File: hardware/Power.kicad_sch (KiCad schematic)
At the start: 41 parts, among them IC1 3.3V/0.5A, IC2 TPS54202HDDCR, U12 LMR33640DDDA

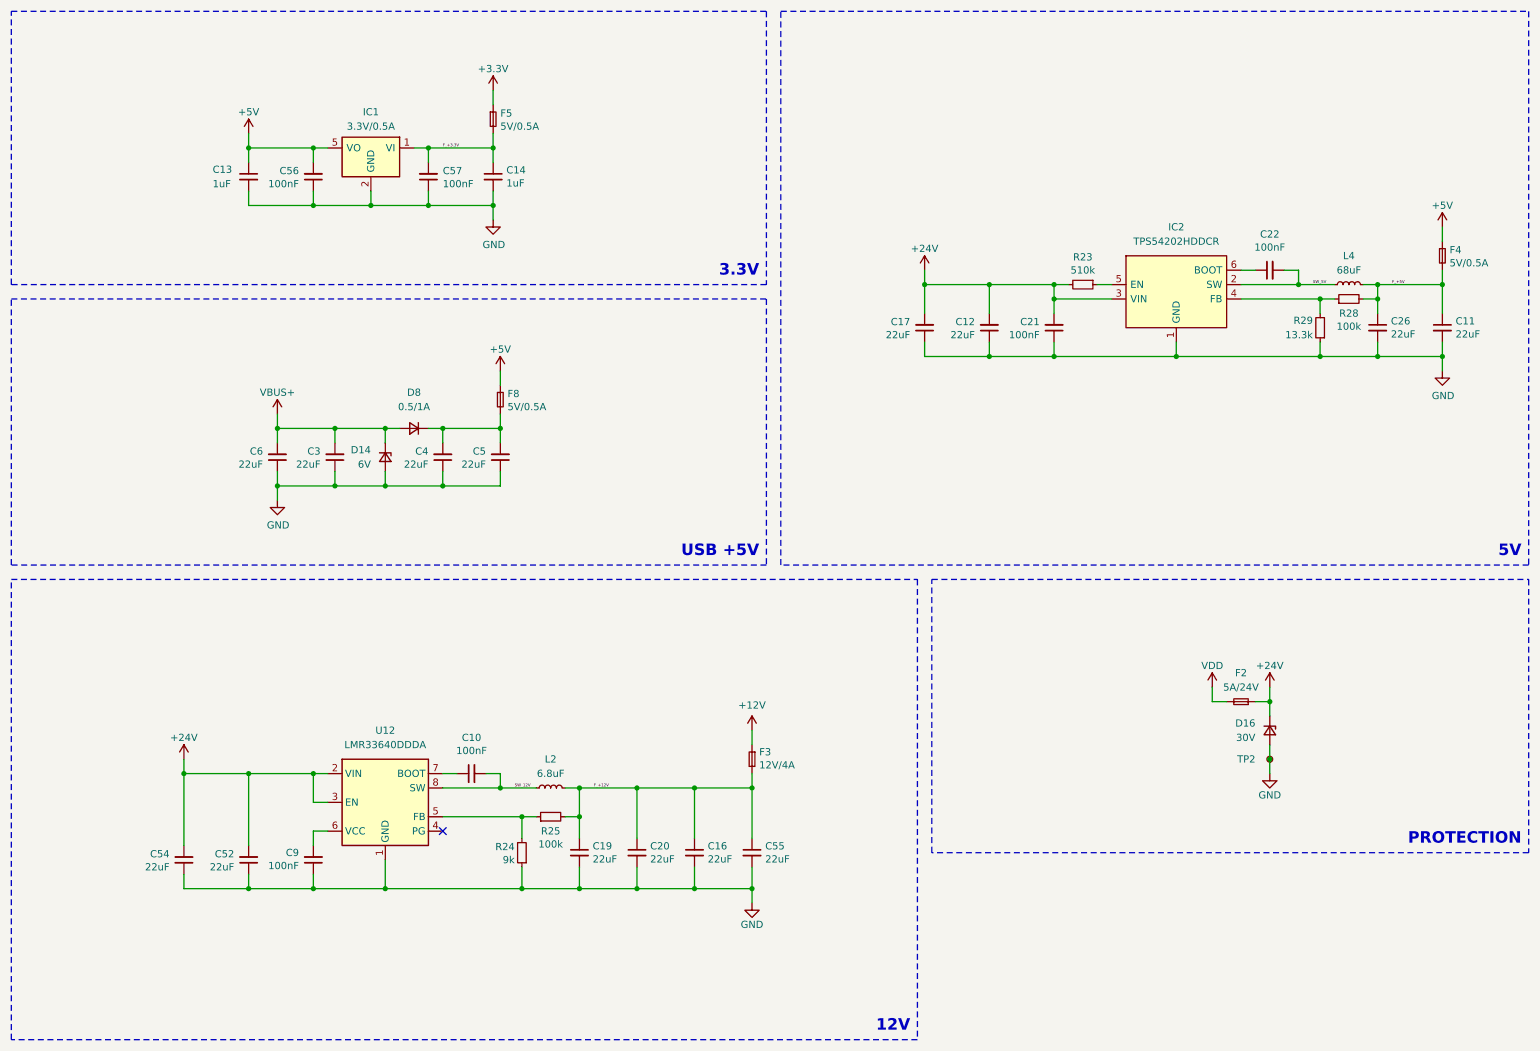
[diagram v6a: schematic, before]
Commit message: inductors 3d models fix, smaller relay (same series as the one from IMD), other + sync
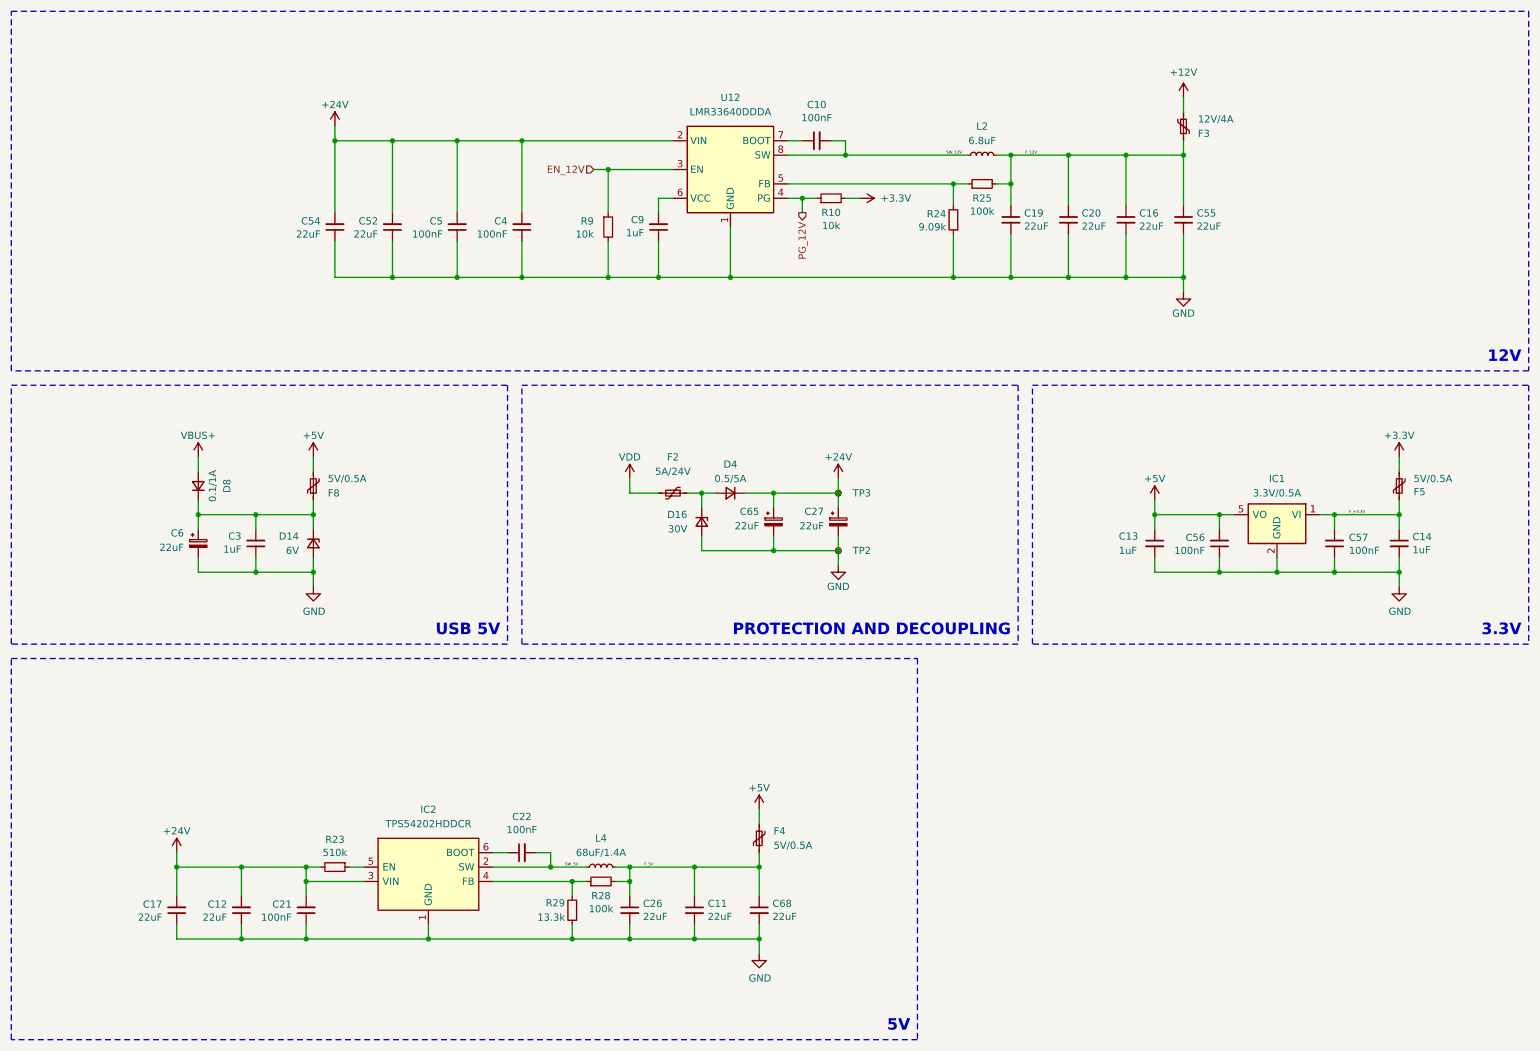
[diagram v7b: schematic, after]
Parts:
- removed C6: 22uF, Capacitor_SMD:C_0805_2012Metric, symbol Device:C_Small
- added C27, C6, C65: 22uF, Capacitor_SMD:CP_Elec_4x5.8, symbol Device:C_Polarized_Small
- added C68: 22uF, Capacitor_SMD:C_0805_2012Metric, symbol Device:C_Small
- added D4: 0.5/5A, symbol Device:D_Small
- added R10, R9: 10k, Resistor_SMD:R_0603_1608Metric, symbol Device:R_Small
- added TP3: TestPoint_Small, TestPoint:TestPoint_Pad_D1.0mm, symbol Connector:TestPoint_Small
- C3: value 22uF -> 1uF; footprint Capacitor_SMD:C_0805_2012Metric -> Capacitor_SMD:C_0603_1608Metric; Manufacturer_Name MCASH21GCC7684MTCA1J -> --; Manufacturer_Part_Number CL21A107MQYNNWE -> C0603C104J3RACTU; Mouser Part Number 187-CL21A107MQYNNWE -> 80-C0603C104J3R; Mouser Price/Stock https://www.mouser.pl/ProductDetail/Samsung-Electro-Mechani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 -> https://www.mouser.pl/ProductDetail/KEMET/C0603C104J3RACTU?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
- C4, C5: value 22uF -> 100nF
- C9: value 100nF -> 1uF
- D8: value 0.5/1A -> 0.1/1A
- F2: symbol Samacsys2:2920L500_24SLDR -> Device:Polyfuse_Small
- F3, F4, F5, F8: symbol Device:Fuse_Small -> Device:Polyfuse_Small
- L4: value 68uF -> 68uF/1.4A
- R24: value 9k -> 9.09k
- TP2: footprint Connector_Pin:Pin_D0.7mm_L6.5mm_W1.8mm_FlatFork -> TestPoint:TestPoint_Pad_D1.0mm
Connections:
- net +24V: now also C4.2, C5.2, C27.1, C65.1, D4.1 (K), TP3.1; no longer D16.1 (K), F2.1, U12.3 (EN)
- net +3.3V: now also F5.2, R10.2; no longer F5.1
- net +5V: now also F4.2, F8.2; no longer F4.1, F8.1
- net F_+3.3V: now also F5.1; no longer F5.2
- net GND: now also C27.2, C6.2, C65.2, C68.2, R9.2
- net VBUS+: no longer C3.2, D14.1 (K)
- net PG_12V: now reaches U12.4 (PG)
- net PG_12V: now also R10.1
- net F_+12V renamed F_12V
- net F_+5V renamed F_5V
- net F_5V: now also F4.1, C68.1; no longer F4.2
- new net: C3.2, C6.1, D14.1 (K), D8.1 (K), F8.1
- new net: D16.1 (K), D4.2 (A), F2.1
- new net EN_12V: R9.1, U12.3 (EN)
- no-connect marks 1 -> 0
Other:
- note added: "PROTECTION AND DECOUPLING"
- note added: "USB 5V"
- note removed: "PROTECTION"
- note removed: "USB +5V"
- moved on the sheet: C10, C11, C12, C13, C14, C16, C17, C19, C20, C21, C22, C26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

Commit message: all but the communications sections done
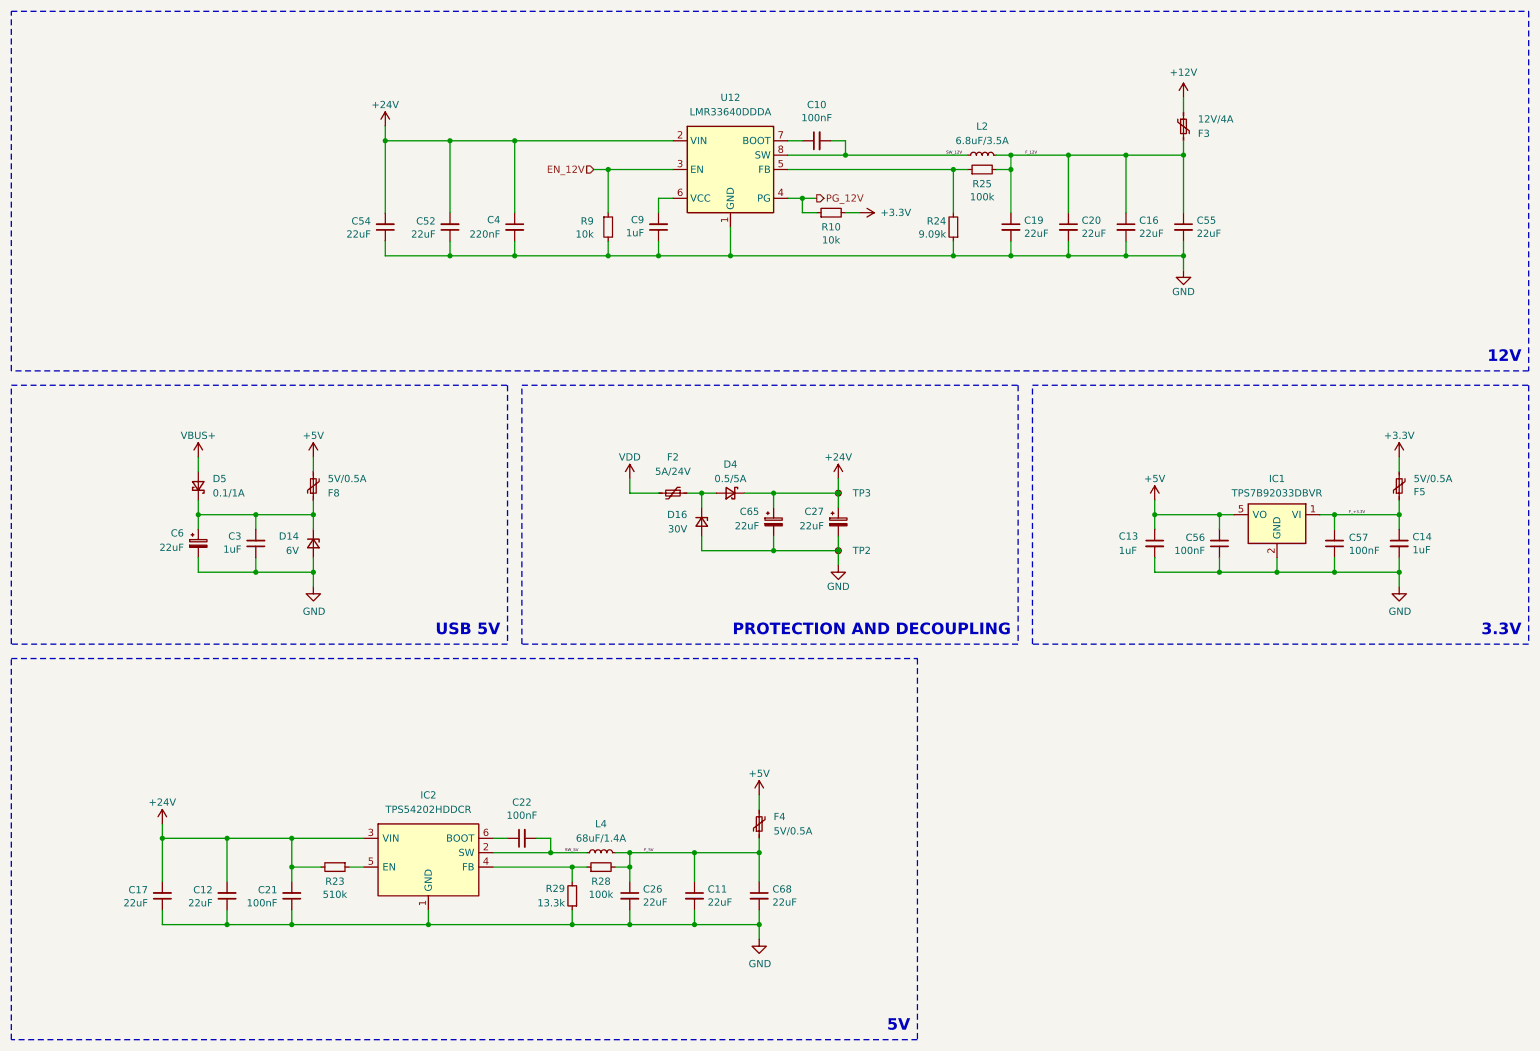
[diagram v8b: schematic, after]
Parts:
- removed C5: 100nF, Capacitor_SMD:C_0805_2012Metric, symbol Device:C_Small
- removed D8: 0.1/1A, symbol Device:D_Small
- added D5: 0.1/1A, Diode_SMD:D_SOD-123, symbol Device:D_Schottky_Small
- C4: value 100nF -> 220nF; footprint Capacitor_SMD:C_0805_2012Metric -> Capacitor_SMD:C_0603_1608Metric; Manufacturer_Name MCASH21GCC7684MTCA1J -> --; Manufacturer_Part_Number CL21A107MQYNNWE -> --; Mouser Part Number 187-CL21A107MQYNNWE -> (none); Mouser Price/Stock https://www.mouser.pl/ProductDetail/Samsung-Electro-Mechani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 -> (none)
- D14, D16: footprint (none) -> Diode_SMD:D_SOD-123
- D4: footprint (none) -> Diode_SMD:D_SOD-123; symbol Device:D_Small -> Device:D_Schottky_Small
- IC1: value 3.3V/0.5A -> TPS7B92033DBVR
- L2: value 6.8uF -> 6.8uF/3.5A
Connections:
- net +24V: now also C4.1; no longer C4.2
- net GND: now also C4.2; no longer C4.1
- net VBUS+: now also D5.2 (A)
- net at C3.2, C6.1, D14.1 (K)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: now also D5.1 (K)
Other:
- moved on the sheet: C11, C12, C16, C17, C19, C20, C21, C22, C26, C52, C54, C55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
